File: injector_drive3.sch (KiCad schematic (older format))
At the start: 17 parts, among them P30 CONN_1, P31 CONN_1, Q14 PIP-3104, Q15 HALL

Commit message: Removed LM1815 options. Now adaptive mode and square waves are the default,
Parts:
- C51: Field1 (none) -> newark,97M4148; Field2 (none) -> vendor1, smd w hem; Field3 (none) -> vendor2, thru w hem; Field4 (none) -> vendor2, smd w hem; Field5 (none) -> 200,V; Field6 (none) -> 10,%; Field7 (none) -> Multilayer Ceramic; Field8 (none) -> other,more,stuff
- D84, D87: Field1 (none) -> vendor1, thru w hem; Field2 (none) -> vendor1, smd w hem; Field3 (none) -> vendor2, thru w hem; Field4 (none) -> vendor2, smd w hem; Field5 (none) -> reverse,V; Field6 (none) -> current,A; Field7 (none) -> x; Field8 (none) -> other,more,stuff
- D85: Field1 (none) -> newark,18M3533; Field2 (none) -> vendor1, smd w hem; Field3 (none) -> vendor2, thru w hem; Field4 (none) -> vendor2, smd w hem; Field5 (none) -> 500,mW; Field6 (none) -> 20,mA; Field7 (none) -> X; Field8 (none) -> other,more,stuff
- D86: Field1 (none) -> newark,58K2469; Field2 (none) -> vendor1, smd w hem; Field3 (none) -> vendor2, thru w hem; Field4 (none) -> vendor2, smd w hem; Field5 (none) -> x,x; Field6 (none) -> x,x; Field7 (none) -> construct; Field8 (none) -> other,more,stuff
- L3: Field1 (none) -> vendor1, thru w hem; Field2 (none) -> vendor1, smd w hem; Field3 (none) -> vendor2, thru w hem; Field4 (none) -> vendor2, smd w hem; Field5 (none) -> x,x; Field6 (none) -> x,x; Field7 (none) -> x; Field8 (none) -> other,more,stuff
- Q14: Field1 (none) -> digi,PIP3104-ND; Field2 (none) -> vendor1, smd w hem; Field3 (none) -> vendor2, thru w hem; Field4 (none) -> vendor2, smd w hem; Field5 (none) -> 8,A; Field6 (none) -> x,x; Field7 (none) -> TOPFET; Field8 (none) -> other,more,stuff
- Q15: Field1 (none) -> digi,480-2002-ND; Field2 (none) -> vendor1, smd w hem; Field3 (none) -> vendor2, thru w hem; Field4 (none) -> vendor2, smd w hem; Field5 (none) -> x,x; Field6 (none) -> x,x; Field7 (none) -> x; Field8 (none) -> other,more,stuff
- R115: Field1 (none) -> newark,38k0327; Field2 (none) -> vendor1, smd w hem; Field3 (none) -> vendor2, thru w hem; Field4 (none) -> vendor2, smd w hem; Field5 (none) -> 250,mW; Field6 (none) -> 5,%; Field7 (none) -> carbon film; Field8 (none) -> other,more,stuff
- R116: Field1 (none) -> newark,38K0329; Field2 (none) -> vendor1, smd w hem; Field3 (none) -> vendor2, thru w hem; Field4 (none) -> vendor2, smd w hem; Field5 (none) -> 250,mW; Field6 (none) -> 5,%; Field7 (none) -> carbon film; Field8 (none) -> other,more,stuff
- R117: Field1 (none) -> newark,38k0352; Field2 (none) -> vendor1, smd w hem; Field3 (none) -> vendor2, thru w hem; Field4 (none) -> vendor2, smd w hem; Field5 (none) -> 250,mW; Field6 (none) -> 5,%; Field7 (none) -> carbon film; Field8 (none) -> other,more,stuff
- R118: Field1 (none) -> vendor1, thru w hem; Field2 (none) -> vendor1, smd w hem; Field3 (none) -> vendor2, thru w hem; Field4 (none) -> vendor2, smd w hem; Field5 (none) -> power,W; Field6 (none) -> tol,%; Field7 (none) -> construct; Field8 (none) -> other,more,stuff
- R119: Field1 (none) -> newark,38K0352; Field2 (none) -> vendor1, smd w hem; Field3 (none) -> vendor2, thru w hem; Field4 (none) -> vendor2, smd w hem; Field5 (none) -> 250,mW; Field6 (none) -> 5,%; Field7 (none) -> carbon film; Field8 (none) -> other,more,stuff
- R120: Field1 (none) -> newark,59K8561; Field2 (none) -> vendor1, smd w hem; Field3 (none) -> vendor2, thru w hem; Field4 (none) -> vendor2, smd w hem; Field5 (none) -> 1,W; Field6 (none) -> 5,%; Field7 (none) -> construct; Field8 (none) -> other,more,stuff
- R121: Field1 (none) -> newark,38K0340; Field2 (none) -> vendor1, smd w hem; Field3 (none) -> vendor2, thru w hem; Field4 (none) -> vendor2, smd w hem; Field5 (none) -> 1/4,W; Field6 (none) -> 5,%; Field7 (none) -> carbon film; Field8 (none) -> other,more,stuff

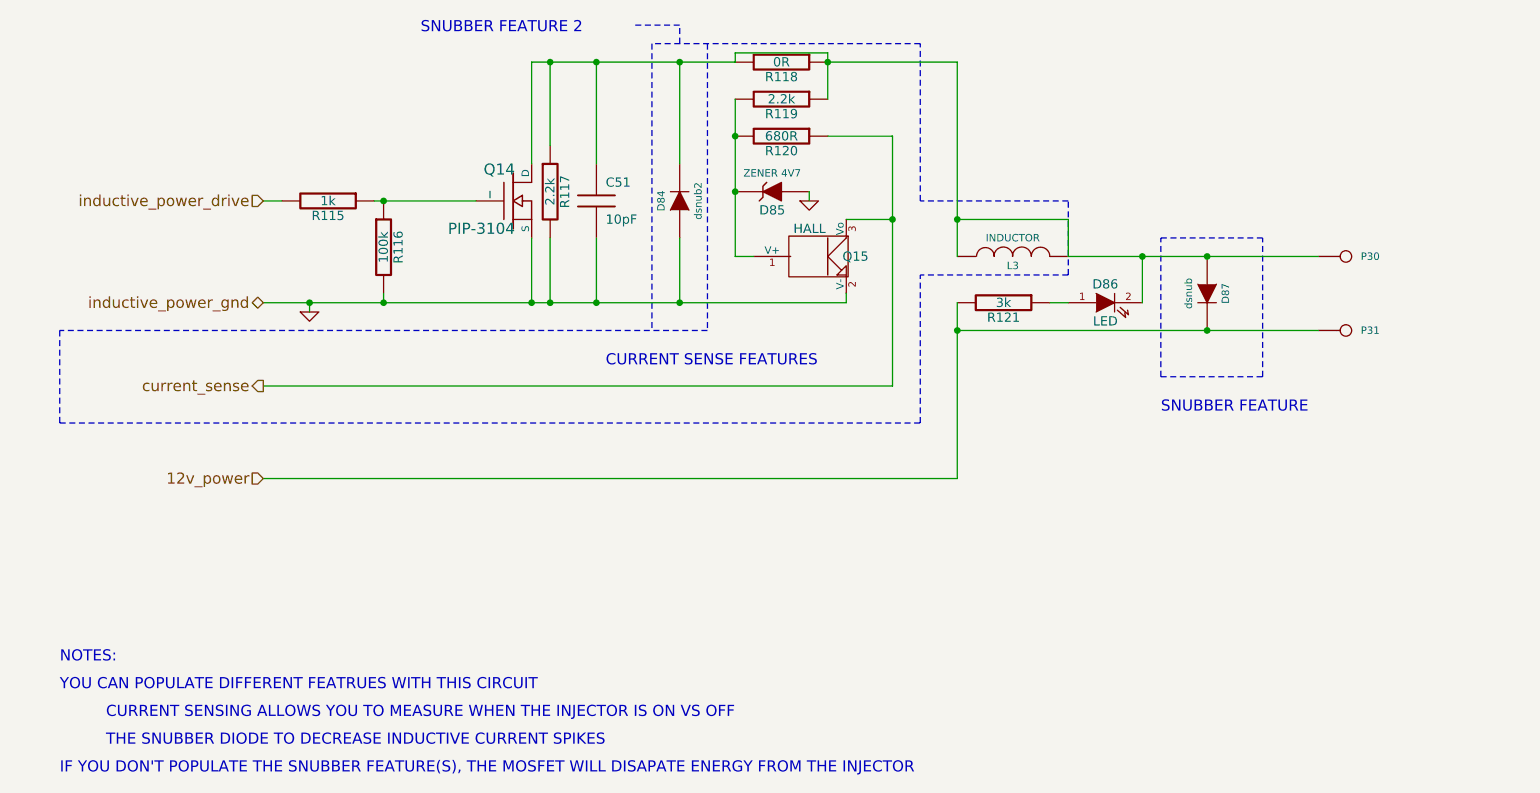
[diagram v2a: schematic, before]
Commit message: Implemented P&H, removed current sense circuitry, removed all unnecessary files from the repo
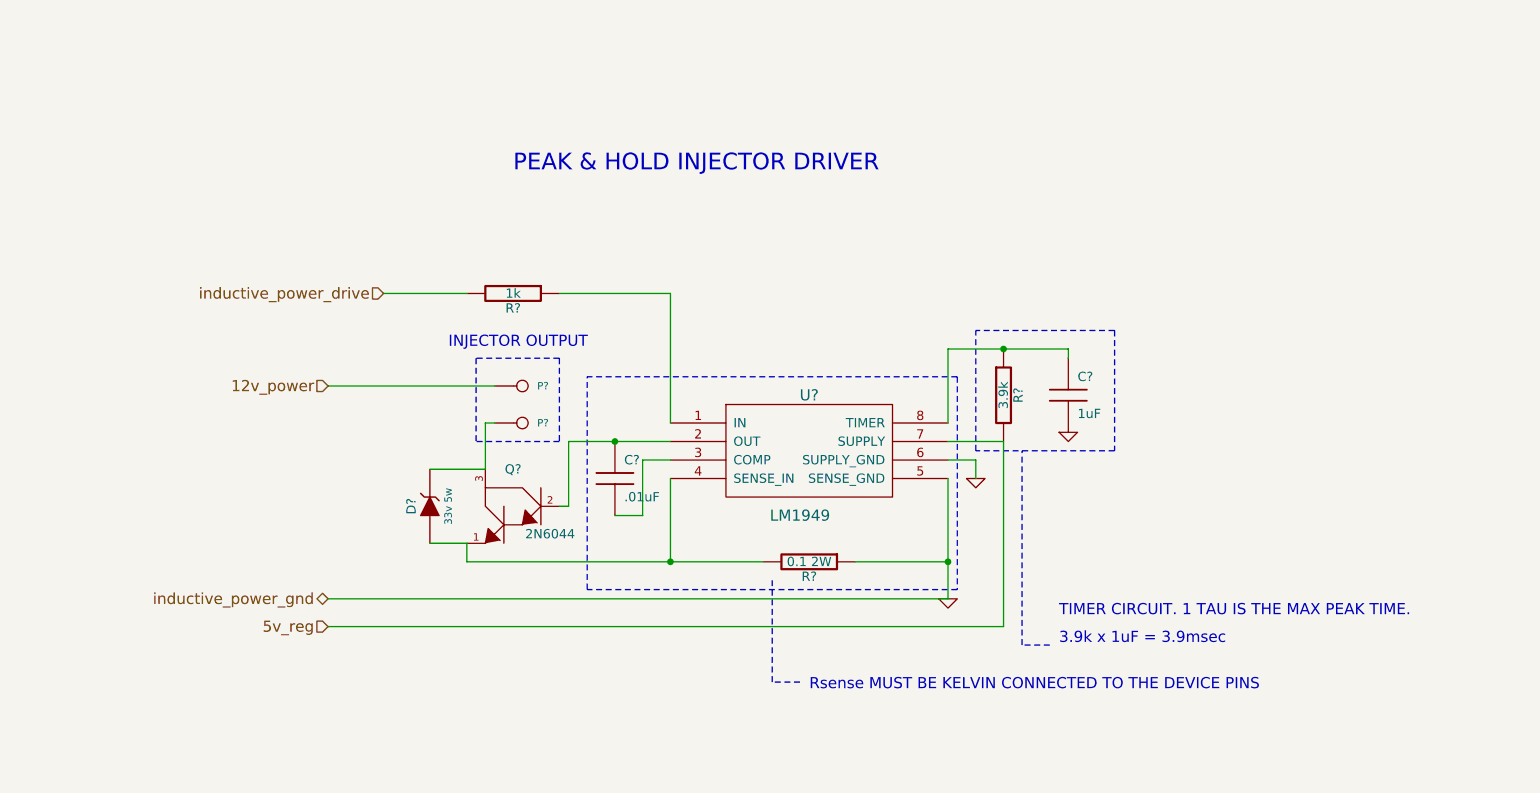
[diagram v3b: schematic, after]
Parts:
- removed C51: 10pF, C1V7, symbol C
- removed D84: dsnub2, D4-SMB, symbol DIODE
- removed D85: ZENER 4V7, D4-SMB, symbol ZENER
- removed D86: LED, LEDV, symbol LED
- removed D87: dsnub, D4-SMB, symbol DIODE
- removed L3: INDUCTOR, SIL-2, symbol INDUCTOR
- removed Q14: PIP-3104, TO220_sm, symbol PIP-3104
- removed Q15: HALL, SIL-3, symbol HALL
- removed R116: 100k, R4-SM0805, symbol R
- removed R117, R119: 2.2k, R4-SM0805, symbol R
- removed R118: 0R, R4-SM0805, symbol R
- removed R120: 680R, R4-SM0805, symbol R
- removed R121: 3k, R4-SM0805, symbol R
- added C?: .01uF, symbol C
- added C?: 1uF, symbol C
- added D?: 33v 5w, symbol ZENER
- added Q?: 2N6044, symbol DARL_N
- added R?: 0.1 2W, symbol R
- added R?: 3.9k, symbol R
- added U?: LM1949, DIP8, symbol LM1949
- renumbered P30 to P?, P31 to P?, R115 to R?
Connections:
- net 12v_power: now also P?.1; no longer P?.1
- net GND: now also C?.2, R?.1, U?.5 (SENSE_GND), U?.6 (SUPPLY_GND)
- net at R?.1: now also U?.1 (IN)
- new net: D?.2 (K), P?.1, Q?.3
- new net: C?.1, Q?.2, U?.2 (OUT)
- new net: C?.2, U?.3 (COMP)
- new net: D?.1 (A), Q?.1, R?.2, U?.4 (SENSE_IN)
- new net: C?.1, R?.1, U?.8 (TIMER)
- new net 5v_reg: R?.2, U?.7 (SUPPLY)
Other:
- note added: "3.9k x 1uF = 3.9msec"
- note added: "INJECTOR OUTPUT"
- note added: "PEAK & HOLD INJECTOR DRIVER"
- note added: "Rsense MUST BE KELVIN CONNECTED TO THE DEVICE PINS"
- note added: "TIMER CIRCUIT. 1 TAU IS THE MAX PEAK TIME."
- note removed: "CURRENT SENSE FEATURES"
- note removed: "CURRENT SENSING ALLOWS YOU TO MEASURE WHEN THE INJECTOR IS ON VS OFF"
- note removed: "IF YOU DON'T POPULATE THE SNUBBER FEATURE(S), THE MOSFET WILL DISAPATE ENERGY FROM THE INJECTOR"
- note removed: "NOTES:"
- note removed: "SNUBBER FEATURE"
- note removed: "SNUBBER FEATURE 2"
- note removed: "THE SNUBBER DIODE TO DECREASE INDUCTIVE CURRENT SPIKES"
- note removed: "YOU CAN POPULATE DIFFERENT FEATRUES WITH THIS CIRCUIT"
- moved on the sheet: P?, R?
